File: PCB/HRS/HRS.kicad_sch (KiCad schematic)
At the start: 16 parts, among them J1 Breakout_Conn, J2 TFT_Conn, SW1 ET02_Power_Switch, U1 TME_1205S

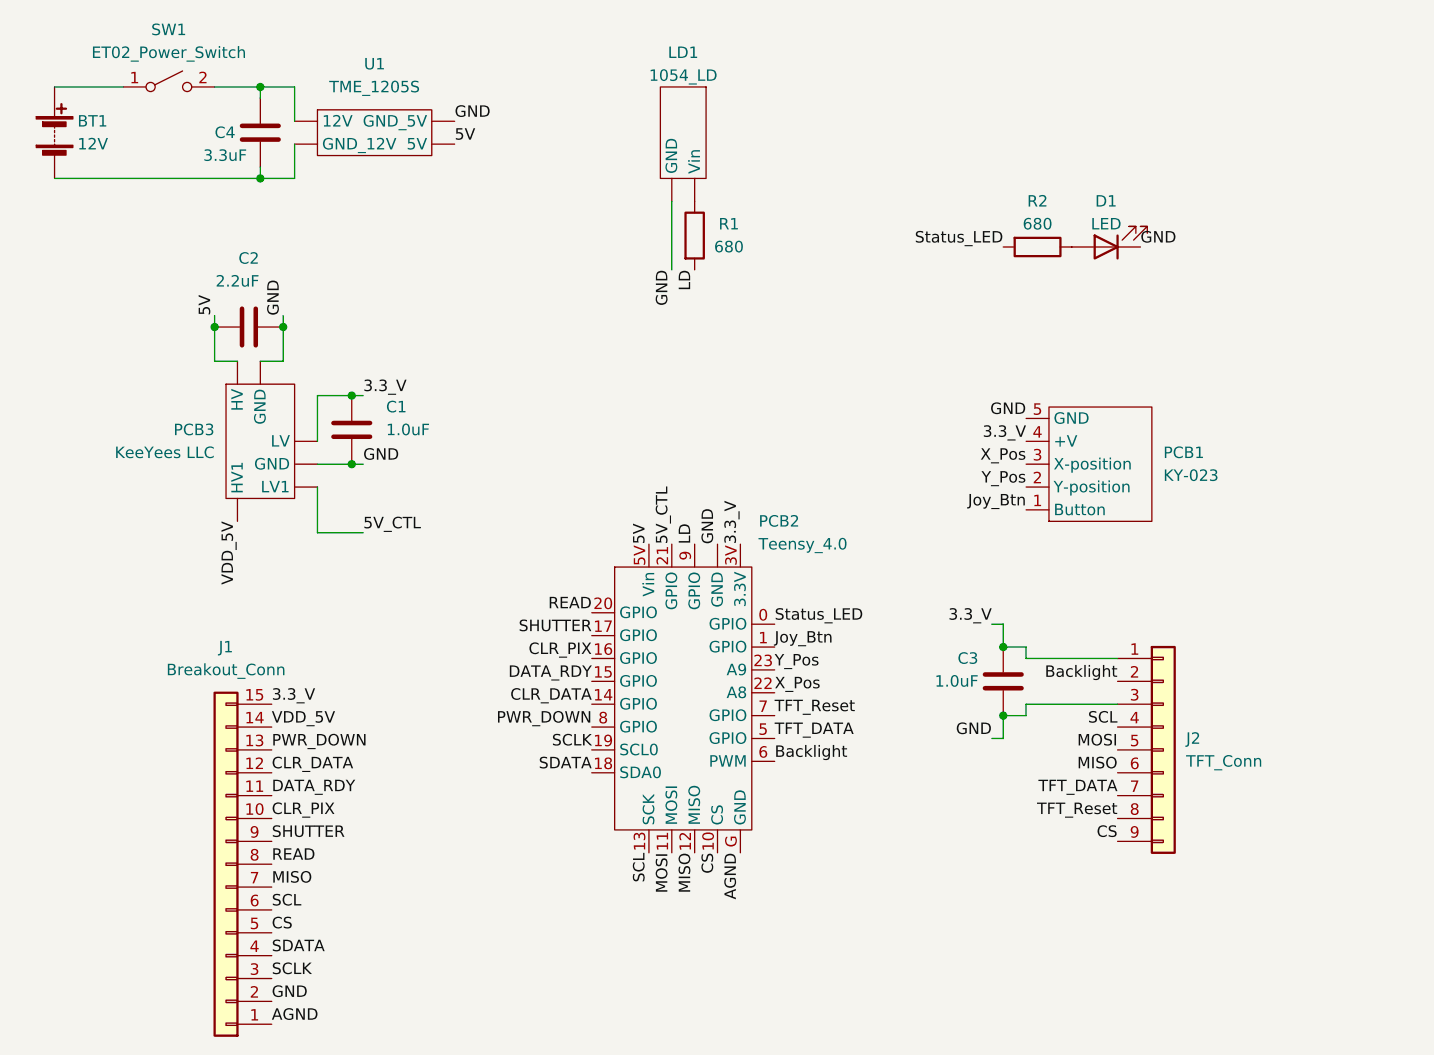
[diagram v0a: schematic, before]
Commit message: Completed footprints and schematics
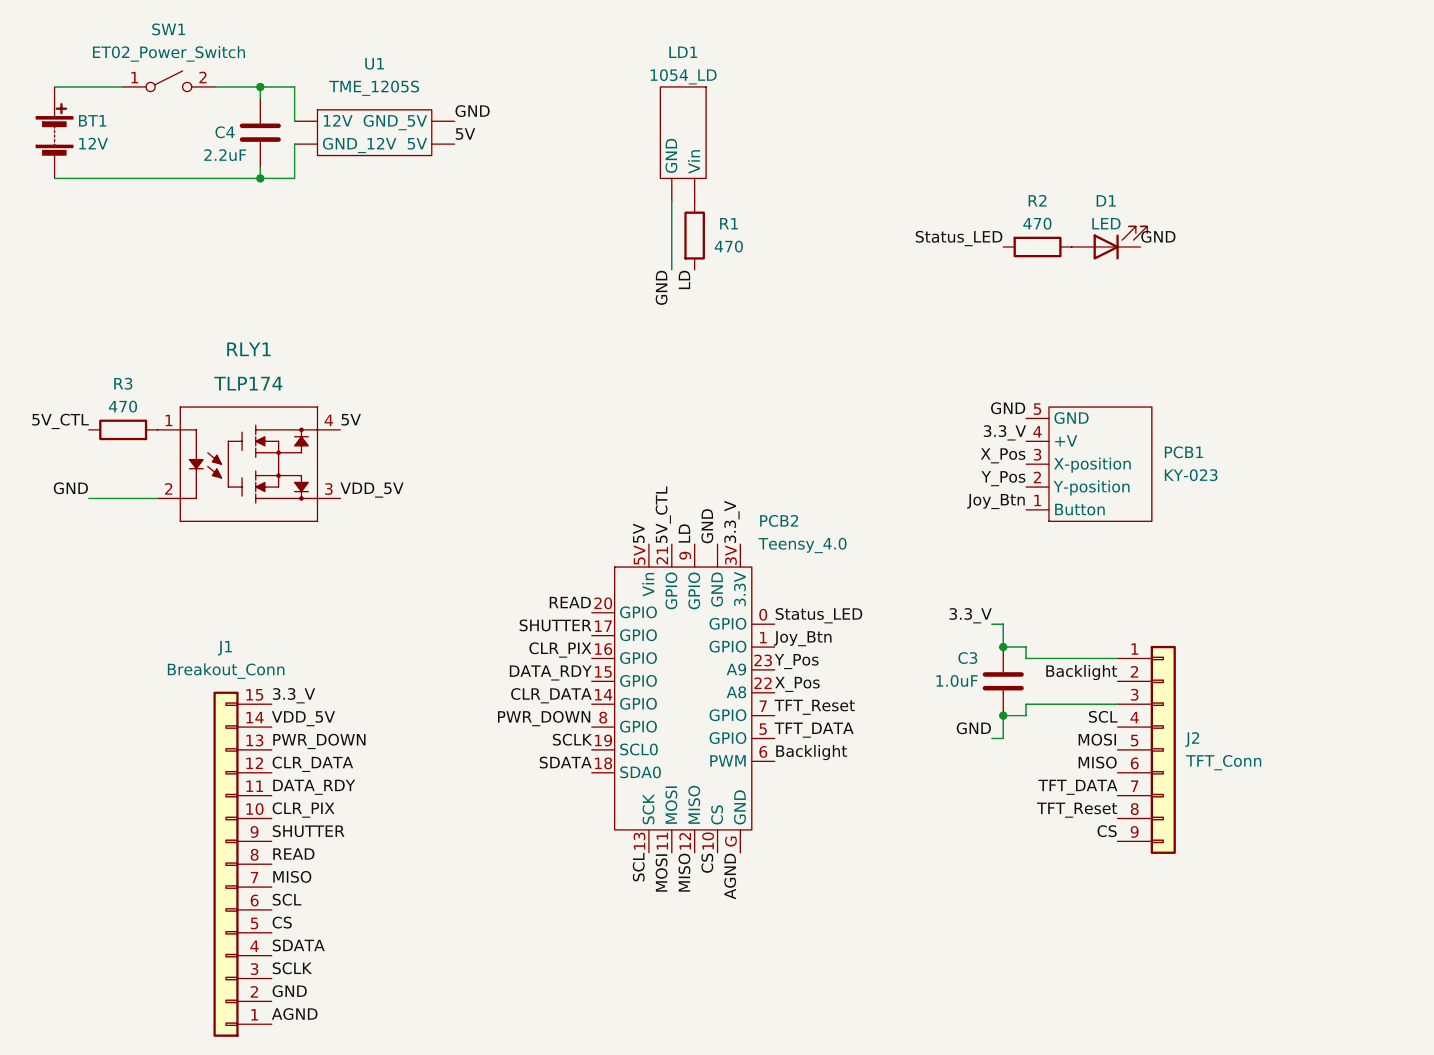
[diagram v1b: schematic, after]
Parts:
- removed C1: 1.0uF, symbol Device:C
- removed C2: 2.2uF, symbol Device:C
- removed PCB3: KeeYees LLC, symbol HRS:KeeYees LLC
- added R3: 470, HRS:R_0603_1608Metric, symbol Device:R
- added RLY1: TLP174, HRS:TLP174, symbol HRS:TLP174
- BT1, LD1: footprint (none) -> HRS:BAT&LD
- C3: footprint (none) -> HRS:C_0603_1608Metric
- C4: value 3.3uF -> 2.2uF; footprint (none) -> HRS:C_0603_1608Metric
- D1: footprint (none) -> HRS:LED_D5.0mm
- J1: footprint (none) -> HRS:Breakout-Connector-Female
- J2: footprint (none) -> HRS:TFT_Conn
- PCB1: footprint (none) -> HRS:Ky-023
- PCB2: footprint (none) -> HRS:Teensy Headers
- R1, R2: value 680 -> 470; footprint (none) -> HRS:R_0603_1608Metric
- SW1: footprint (none) -> HRS:ET02
- U1: footprint (none) -> HRS:TME 1205S
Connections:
- net 5V: now also RLY1.4
- net 5V_CTL: now also R3.1
- net GND: now also RLY1.2
- net VDD_5V: now also RLY1.3
- new net: R3.2, RLY1.1

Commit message: Added resistor for TFT backlight
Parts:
- added R4: 470, HRS:R_0603_1608Metric, symbol Device:R
- renumbered C3 to C1, C4 to C2
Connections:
- net Backlight: now also R4.2; no longer J2.2 (Pin_2)
- new net: J2.2 (Pin_2), R4.1
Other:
- moved on the sheet: C1, J2
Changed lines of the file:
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@@
   (junction (at 91.44 46.99) (diameter 0) (color 0 0 0 0)
   )
+  (junction (at 180.34 99.06) (diameter 0) (color 0 0 0 0)
+  )
   (junction (at 91.44 36.83) (diameter 0) (color 0 0 0 0)
   )
-  (junction (at 173.99 99.06) (diameter 0) (color 0 0 0 0)
-  )
-  (junction (at 173.99 106.68) (diameter 0) (color 0 0 0 0)
+  (junction (at 180.34 106.68) (diameter 0) (color 0 0 0 0)
   )
   (wire (pts (xy 91.44 36.83) (xy 95.25 36.83))
     (stroke (width 0) (type default) (color 0 0 0 0))
   )
+  (wire (pts (xy 180.34 99.06) (xy 191.77 99.06))
+    (stroke (width 0) (type default) (color 0 0 0 0))
+  )
   (wire (pts (xy 72.39 82.55) (xy 80.01 82.55))
     (stroke (width 0) (type default) (color 0 0 0 0))
   )
-  (wire (pts (xy 172.72 96.52) (xy 173.99 96.52))
+  (wire (pts (xy 176.53 96.52) (xy 177.8 96.52))
     (stroke (width 0) (type default) (color 0 0 0 0))
   )
@@
     (stroke (width 0) (type default) (color 0 0 0 0))
   )
-  (wire (pts (xy 176.53 100.33) (xy 176.53 99.06))
+  (wire (pts (xy 177.8 99.06) (xy 180.34 99.06))
+    (stroke (width 0) (type default) (color 0 0 0 0))
+  )
+  (wire (pts (xy 191.77 100.33) (xy 191.77 99.06))
     (stroke (width 0) (type default) (color 0 0 0 0))
   )
@@
     (stroke (width 0) (type default) (color 0 0 0 0))
   )
-  (wire (pts (xy 173.99 99.06) (xy 176.53 99.06))
-    (stroke (width 0) (type default) (color 0 0 0 0))
-  )
   (wire (pts (xy 95.25 40.64) (xy 95.25 36.83))
     (stroke (width 0) (type default) (color 0 0 0 0))
   )
-  (wire (pts (xy 172.72 109.22) (xy 173.99 109.22))
+  (wire (pts (xy 176.53 109.22) (xy 177.8 109.22))
     (stroke (width 0) (type default) (color 0 0 0 0))
   )
@@
     (stroke (width 0) (type default) (color 0 0 0 0))
   )
-  (wire (pts (xy 186.69 100.33) (xy 176.53 100.33))
-    (stroke (width 0) (type default) (color 0 0 0 0))
-  )
-  (wire (pts (xy 173.99 109.22) (xy 173.99 106.68))
+  (wire (pts (xy 180.34 106.68) (xy 191.77 106.68))
+    (stroke (width 0) (type default) (color 0 0 0 0))
+  )
+  (wire (pts (xy 201.93 100.33) (xy 191.77 100.33))
+    (stroke (width 0) (type default) (color 0 0 0 0))
+  )
+  (wire (pts (xy 177.8 109.22) (xy 177.8 106.68))
     (stroke (width 0) (type default) (color 0 0 0 0))
   )
@@
     (stroke (width 0) (type default) (color 0 0 0 0))
   )
-  (wire (pts (xy 173.99 96.52) (xy 173.99 99.06))
-    (stroke (width 0) (type default) (color 0 0 0 0))
-  )
-  (wire (pts (xy 176.53 105.41) (xy 176.53 106.68))
+  (wire (pts (xy 177.8 96.52) (xy 177.8 99.06))
+    (stroke (width 0) (type default) (color 0 0 0 0))
+  )
+  (wire (pts (xy 191.77 105.41) (xy 191.77 106.68))
+    (stroke (width 0) (type default) (color 0 0 0 0))
+  )
+  (wire (pts (xy 177.8 106.68) (xy 180.34 106.68))
     (stroke (width 0) (type default) (color 0 0 0 0))
   )
@@
     (stroke (width 0) (type default) (color 0 0 0 0))
   )
-  (wire (pts (xy 176.53 106.68) (xy 173.99 106.68))
-    (stroke (width 0) (type default) (color 0 0 0 0))
-  )
-  (wire (pts (xy 186.69 105.41) (xy 176.53 105.41))
+  (wire (pts (xy 201.93 105.41) (xy 191.77 105.41))
     (stroke (width 0) (type default) (color 0 0 0 0))
   )
@@
     (effects (font (size 1.27 1.27)) (justify left bottom))
   )
-  (label "Backlight" (at 186.69 102.87 180)
+  (label "Backlight" (at 194.31 102.87 180)
     (effects (font (size 1.27 1.27)) (justify right bottom))
   )
@@
     (effects (font (size 1.27 1.27)) (justify left bottom))
   )
-  (label "TFT_DATA" (at 186.69 115.57 180)
+  (label "TFT_DATA" (at 201.93 115.57 180)
     (effects (font (size 1.27 1.27)) (justify right bottom))
   )
@@
     (effects (font (size 1.27 1.27)) (justify right bottom))
   )
-  (label "MOSI" (at 186.69 110.49 180)
+  (label "MOSI" (at 201.93 110.49 180)
     (effects (font (size 1.27 1.27)) (justify right bottom))
   )
@@
     (effects (font (size 1.27 1.27)) (justify right bottom))
   )
-  (label "TFT_Reset" (at 186.69 118.11 180)
-    (effects (font (size 1.27 1.27)) (justify right bottom))
-  )
-  (label "SCL" (at 186.69 107.95 180)
+  (label "TFT_Reset" (at 201.93 118.11 180)
+    (effects (font (size 1.27 1.27)) (justify right bottom))
+  )
+  (label "SCL" (at 201.93 107.95 180)
     (effects (font (size 1.27 1.27)) (justify right bottom))
   )
@@
     (effects (font (size 1.27 1.27)) (justify left bottom))
   )
-  (label "CS" (at 186.69 120.65 180)
-    (effects (font (size 1.27 1.27)) (justify right bottom))
-  )
-  (label "GND" (at 172.72 109.22 180)
+  (label "CS" (at 201.93 120.65 180)
+    (effects (font (size 1.27 1.27)) (justify right bottom))
+  )
+  (label "GND" (at 176.53 109.22 180)
     (effects (font (size 1.27 1.27)) (justify right bottom))
   )
@@
     (effects (font (size 1.27 1.27)) (justify left bottom))
   )
-  (label "MISO" (at 186.69 113.03 180)
+  (label "MISO" (at 201.93 113.03 180)
     (effects (font (size 1.27 1.27)) (justify right bottom))
   )
@@
     (effects (font (size 1.27 1.27)) (justify right bottom))
   )
-  (label "3.3_V" (at 172.72 96.52 180)
+  (label "3.3_V" (at 176.53 96.52 180)
     (effects (font (size 1.27 1.27)) (justify right bottom))
   )
@@
     (effects (font (size 1.27 1.27)) (justify left bottom))
   )
-  (symbol (lib_id "Connector_Generic:Conn_01x09") (at 191.77 110.49 0) (unit 1)
-    (in_bom yes) (on_board yes) (fields_autoplaced)
-    (property "Reference" "J2" (id 0) (at 194.31 109.2199 0)
+  (symbol (lib_id "Connector_Generic:Conn_01x09") (at 207.01 110.49 0) (unit 1)
+    (in_bom yes) (on_board yes) (fields_autoplaced)
+    (property "Reference" "J2" (id 0) (at 209.55 109.2199 0)
       (effects (font (size 1.27 1.27)) (justify left))
     )
-    (property "Value" "TFT_Conn" (id 1) (at 194.31 111.7599 0)
+    (property "Value" "TFT_Conn" (id 1) (at 209.55 111.7599 0)
       (effects (font (size 1.27 1.27)) (justify left))
     )
-    (property "Footprint" "HRS:TFT_Conn" (id 2) (at 191.77 110.49 0)
-      (effects (font (size 1.27 1.27)) hide)
-    )
-    (property "Datasheet" "~" (id 3) (at 191.77 110.49 0)
+    (property "Footprint" "HRS:TFT_Conn" (id 2) (at 207.01 110.49 0)
+      (effects (font (size 1.27 1.27)) hide)
+    )
+    (property "Datasheet" "~" (id 3) (at 207.01 110.49 0)
       (effects (font (size 1.27 1.27)) hide)
     )
@@
   (symbol (lib_id "Device:C") (at 91.44 41.91 180) (unit 1)
     (in_bom yes) (on_board yes)
-    (property "Reference" "C4" (id 0) (at 86.36 41.91 0)
+    (property "Reference" "C2" (id 0) (at 86.36 41.91 0)
       (effects (font (size 1.27 1.27)) (justify right))
     )
@@
     (pin "2")
   )
-  (symbol (lib_id "Device:C") (at 173.99 102.87 180) (unit 1)
-    (in_bom yes) (on_board yes)
-    (property "Reference" "C3" (id 0) (at 168.91 100.33 0)
+  (symbol (lib_id "Device:C") (at 180.34 102.87 180) (unit 1)
+    (in_bom yes) (on_board yes)
+    (property "Reference" "C1" (id 0) (at 173.99 100.33 0)
       (effects (font (size 1.27 1.27)) (justify right))
     )
-    (property "Value" "1.0uF" (id 1) (at 166.37 102.87 0)
+    (property "Value" "1.0uF" (id 1) (at 171.45 102.87 0)
       (effects (font (size 1.27 1.27)) (justify right))
     )
-    (property "Footprint" "HRS:C_0603_1608Metric" (id 2) (at 173.0248 99.06 0)
-      (effects (font (size 1.27 1.27)) hide)
-    )
-    (property "Datasheet" "~" (id 3) (at 173.99 102.87 0)
+    (property "Footprint" "HRS:C_0603_1608Metric" (id 2) (at 179.3748 99.06 0)
+      (effects (font (size 1.27 1.27)) hide)
+    )
+    (property "Datasheet" "~" (id 3) (at 180.34 102.87 0)
       (effects (font (size 1.27 1.27)) hide)
     )
@@
     )
     (property "Datasheet" "~" (id 3) (at 185.42 54.61 0)
+      (effects (font (size 1.27 1.27)) hide)
+    )
+    (pin "1")
+    (pin "2")
+  )
+  (symbol (lib_id "Device:R") (at 198.12 102.87 270) (unit 1)
+    (in_bom yes) (on_board yes)
+    (property "Reference" "R4" (id 0) (at 198.12 96.52 90))
+    (property "Value" "470" (id 1) (at 198.12 99.06 90))
+    (property "Footprint" "HRS:R_0603_1608Metric" (id 2) (at 198.12 101.092 90)
+      (effects (font (size 1.27 1.27)) hide)
+    )
+    (property "Datasheet" "~" (id 3) (at 198.12 102.87 0)
       (effects (font (size 1.27 1.27)) hide)
     )
@@
     )
     (path "/16a14466-4534-4408-b86a-2b45515f93bb"
-      (reference "C3") (unit 1) (value "1.0uF") (footprint "HRS:C_0603_1608Metric")
+      (reference "C1") (unit 1) (value "1.0uF") (footprint "HRS:C_0603_1608Metric")
     )
     (path "/0c172e39-fd2c-4367-980d-b2af94c7ea0b"
-      (reference "C4") (unit 1) (value "2.2uF") (footprint "HRS:C_0603_1608Metric")
+      (reference "C2") (unit 1) (value "2.2uF") (footprint "HRS:C_0603_1608Metric")
     )
     (path "/3283a0a5-2fd9-4cdb-a039-488df45766ee"
@@
       (reference "R3") (unit 1) (value "470") (footprint "HRS:R_0603_1608Metric")
     )
+    (path "/3293de8d-624d-4c14-a62a-a8c9af69b1b7"
+      (reference "R4") (unit 1) (value "470") (footprint "HRS:R_0603_1608Metric")
+    )
     (path "/fe1ea0e3-12a5-48c7-8d36-820efe655171"
